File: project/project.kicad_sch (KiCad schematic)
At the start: 28 parts, among them J101 BUS, J102 BUS, J103 Back, J104 Front, J105 FFC, SW101 SW_DIP_x04, U101 GX101, U102 GX101

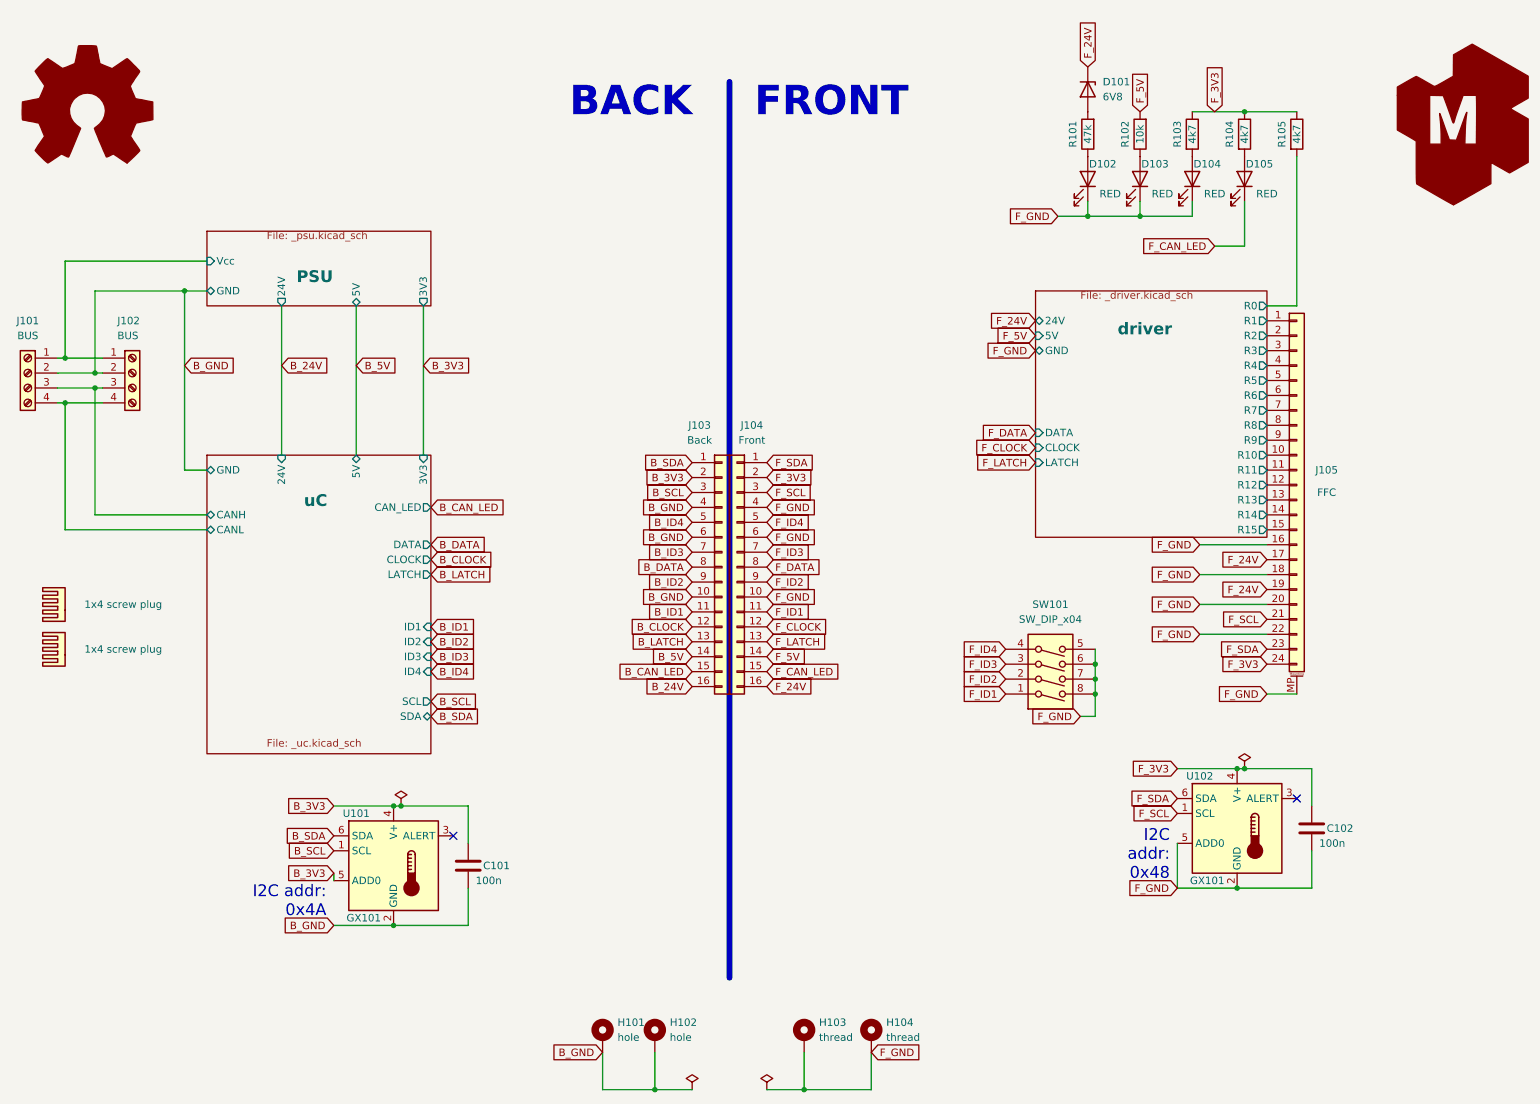
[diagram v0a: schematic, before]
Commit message: spritting up boards into separate repos
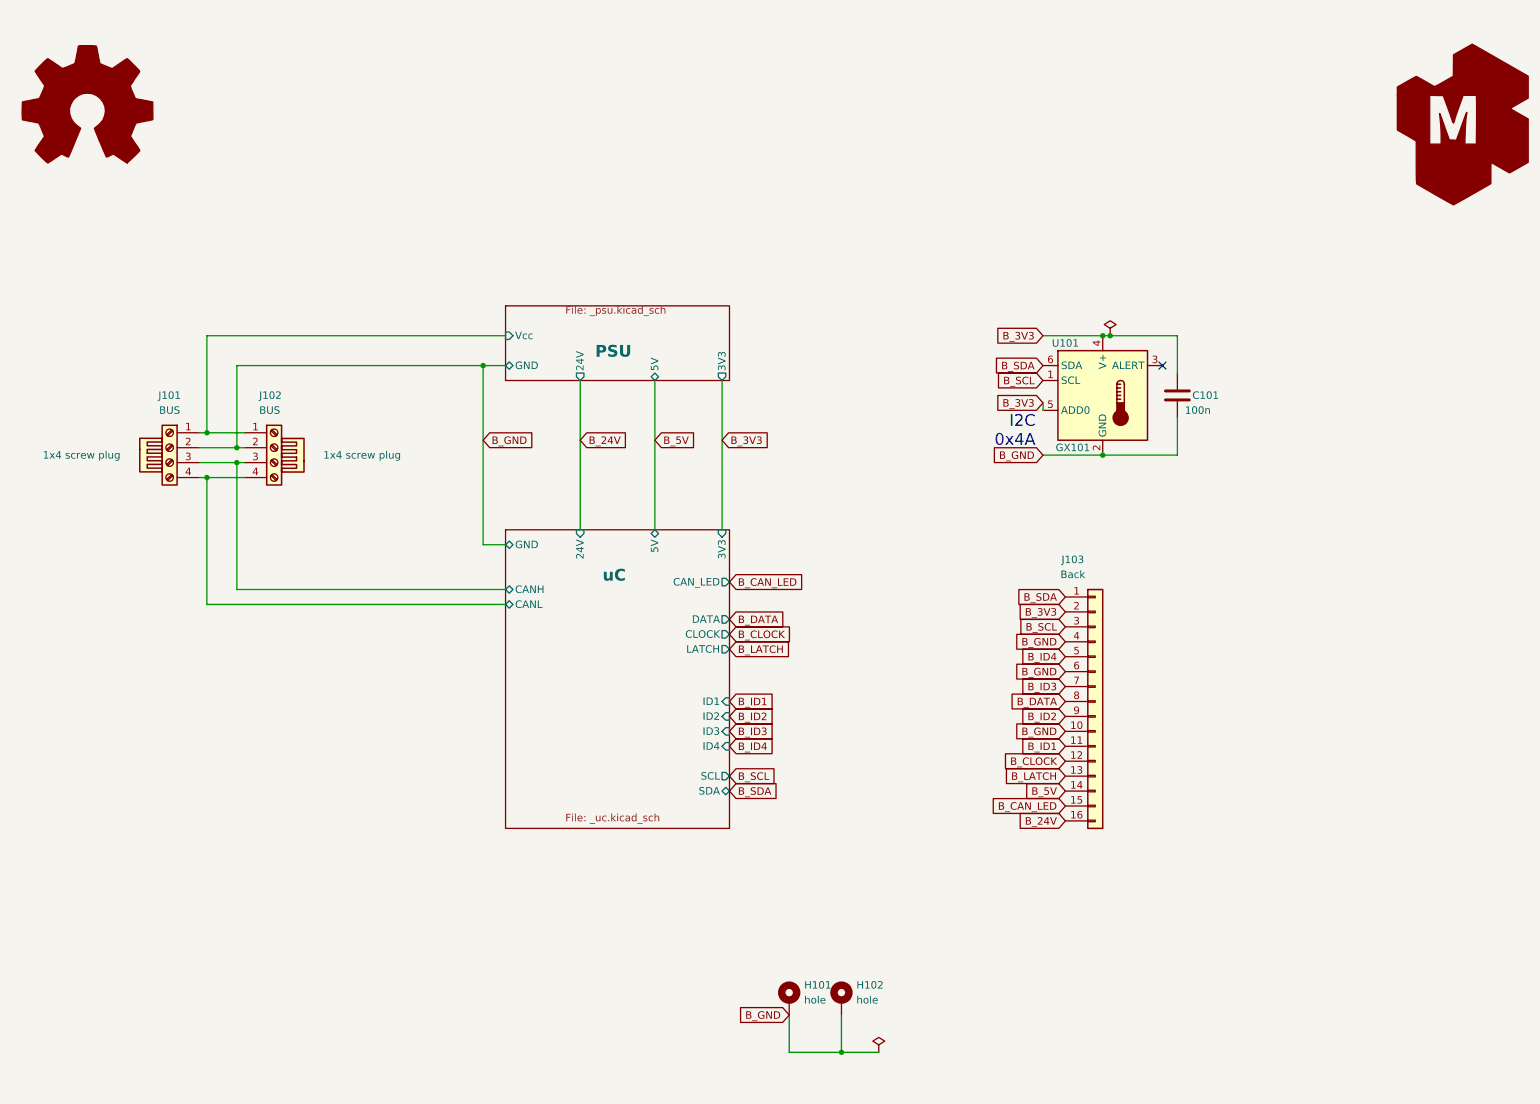
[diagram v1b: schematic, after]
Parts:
- removed C102: 100n, Capacitor_SMD:C_0805_2012Metric_Pad1.18x1.45mm_HandSolder, symbol Device:C
- removed D101: 6V8, Diode_SMD:D_SOD-323_HandSoldering, symbol Device:D_Zener
- removed D102, D103, D104, D105: RED, -local:LED_1206_3216Metric_ReverseMount, symbol Device:LED
- removed H103, H104: thread, -local:post_m3x12.5mm, symbol Mechanical:MountingHole_Pad
- removed J104: Front, Connector_PinHeader_2.54mm:PinHeader_2x08_P2.54mm_Vertical_SMD, symbol Connector_Generic:Conn_01x16
- removed J105: FFC, -local:AFC11-S24ICC-00, symbol Connector_Generic_MountingPin:Conn_01x24_MountingPin
- removed R101: 47k, Resistor_SMD:R_0805_2012Metric_Pad1.20x1.40mm_HandSolder, symbol Device:R
- removed R102: 10k, Resistor_SMD:R_0805_2012Metric_Pad1.20x1.40mm_HandSolder, symbol Device:R
- removed R103, R104, R105: 4k7, Resistor_SMD:R_0805_2012Metric_Pad1.20x1.40mm_HandSolder, symbol Device:R
- removed SW101: SW_DIP_x04, -local:SW_DIP_SPSTx04_Slide_6.2x11.16mm_P2.54mm, symbol Switch:SW_DIP_x04
- removed U102: GX101, Package_TO_SOT_SMD:SOT-23-6, symbol Sensor_Temperature:TMP101
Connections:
- no-connect marks 2 -> 1
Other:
- removed sheet driver
- note added: "I2C 0x4A"
- note removed: "BACK"
- note removed: "FRONT"
- note removed: "I2C addr: 0x48"
- note removed: "I2C addr: 0x4A"
- title: WormControl-Relay15x5t15-ControlUI -> WormControl-Relay15x5t15-ControlBoard
- moved on the sheet: C101, H101, H102, J101, J102, J103, U101

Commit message: part consolidation and QoL improvements
* Using same crystal as in other projects
* Switching to TMP102 as TMP101 is no longer available
* Adding cutouts to make assembly esier
* Making net names more readable
* bumping up version
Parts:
- U101: value GX101 -> TMP102; footprint Package_TO_SOT_SMD:SOT-23-6 -> -local:SOT-563; lcsc# C5441728 -> C99269
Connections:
- net B_24V renamed 24V
- net B_3V3 renamed 3V3
- net B_5V renamed 5V
- net B_CAN_LED renamed CAN_LED
- net B_CLOCK renamed CLOCK
- net B_DATA renamed DATA
- net B_GND renamed GND
- net B_ID1 renamed ID1
- net B_ID2 renamed ID2
- net B_ID3 renamed ID3
- net B_ID4 renamed ID4
- net B_LATCH renamed LATCH
- net B_SCL renamed SCL
- net B_SDA renamed SDA

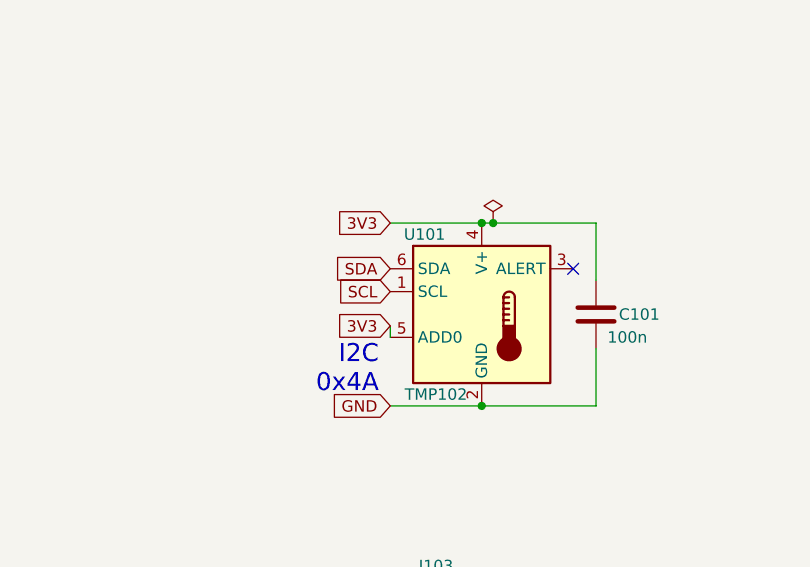
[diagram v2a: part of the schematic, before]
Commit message: fixing tmp102 pinout
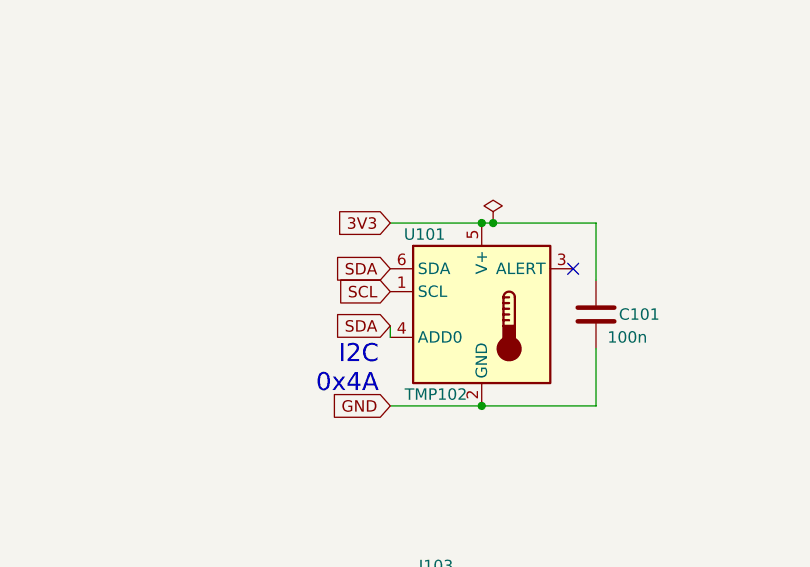
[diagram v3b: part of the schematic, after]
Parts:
- U101: symbol Sensor_Temperature:TMP101 -> Sensor_Temperature:TMP102xxDRL
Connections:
- net 3V3: no longer U101.4 (V+)
- net SDA: now also U101.4 (ADD0)
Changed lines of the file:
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@@
   (title_block
     (title "WormControl-Relay15x5t15-ControlBoard")
-    (date "2026-03-19")
-    (rev "0.5")
+    (date "2026-04-20")
+    (rev "0.6")
     (company "makerspace.lt")
   )
@@
     )
   )
+  (global_label "SDA" (shape input) (at 193.04 80.01 180) (fields_autoplaced)
+    (effects (font (size 1.27 1.27)) (justify right))
+    (property "Intersheet References" "${INTERSHEET_REFS}" (id 0) (at 187.0588 79.9306 0)
+      (effects (font (size 1.27 1.27)) (justify right) hide)
+    )
+  )
   (global_label "SDA" (shape input) (at 196.85 113.03 180) (fields_autoplaced)
     (effects (font (size 1.27 1.27)) (justify right))
@@
     (property "Intersheet References" "${INTERSHEET_REFS}" (id 0) (at 120.2207 86.2806 0)
       (effects (font (size 1.27 1.27)) (justify left) hide)
-    )
-  )
-  (global_label "3V3" (shape input) (at 193.04 80.01 180) (fields_autoplaced)
-    (effects (font (size 1.27 1.27)) (justify right))
-    (property "Intersheet References" "${INTERSHEET_REFS}" (id 0) (at 187.1193 79.9306 0)
-      (effects (font (size 1.27 1.27)) (justify right) hide)
     )
   )
@@
     )
   )
-  (symbol (lib_id "Sensor_Temperature:TMP101") (at 203.2 78.74 0) (unit 1)
+  (symbol (lib_id "Sensor_Temperature:TMP102xxDRL") (at 203.2 78.74 0) (unit 1)
     (in_bom yes) (on_board yes)
     (property "Reference" "U101" (id 0) (at 196.85 69.85 0))
@@
       (effects (font (size 1.27 1.27)) (justify left) hide)
     )
-    (property "Datasheet" "https://www.lcsc.com/datasheet/C99269.pdf" (id 3) (at 204.47 90.17 0)
-      (effects (font (size 1.27 1.27)) (justify left) hide)
-    )
+    (property "Datasheet" "https://www.ti.com/lit/ds/symlink/tmp102.pdf" (id 3) (at 204.47 90.17 0)
+      (effects (font (size 1.27 1.27)) (justify left) hide)
+    )
